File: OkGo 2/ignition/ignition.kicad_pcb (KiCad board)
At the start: 2 copper layers, 167.9 x 105.9 mm, 112 parts, among them K201 16A SPST, K202 16A SPST, K203 16A SPST, K204 16A SPST, K205 16A SPST, M3_MOUNT VAL**, P105 BATT, P107 ARM_LED, P109 BUZZ, P111 SMA, P201 CH3_LED, P203 CH3, P204 CH1_LED, P206 CH1, P207 CH4_LED, P209 CH4, P210 CH2_LED, P212 CH2, Q101 BSS138BK, Q201 BSS138BK, Q202 BSS138BK, Q203 BSS138BK, Q204 BSS138BK, Q205 BSS138BK, U103 SWD, U105 RFM95W, U106 STM32F071CBT6, U107 TSR 0.5-2433, Y101 8MHz

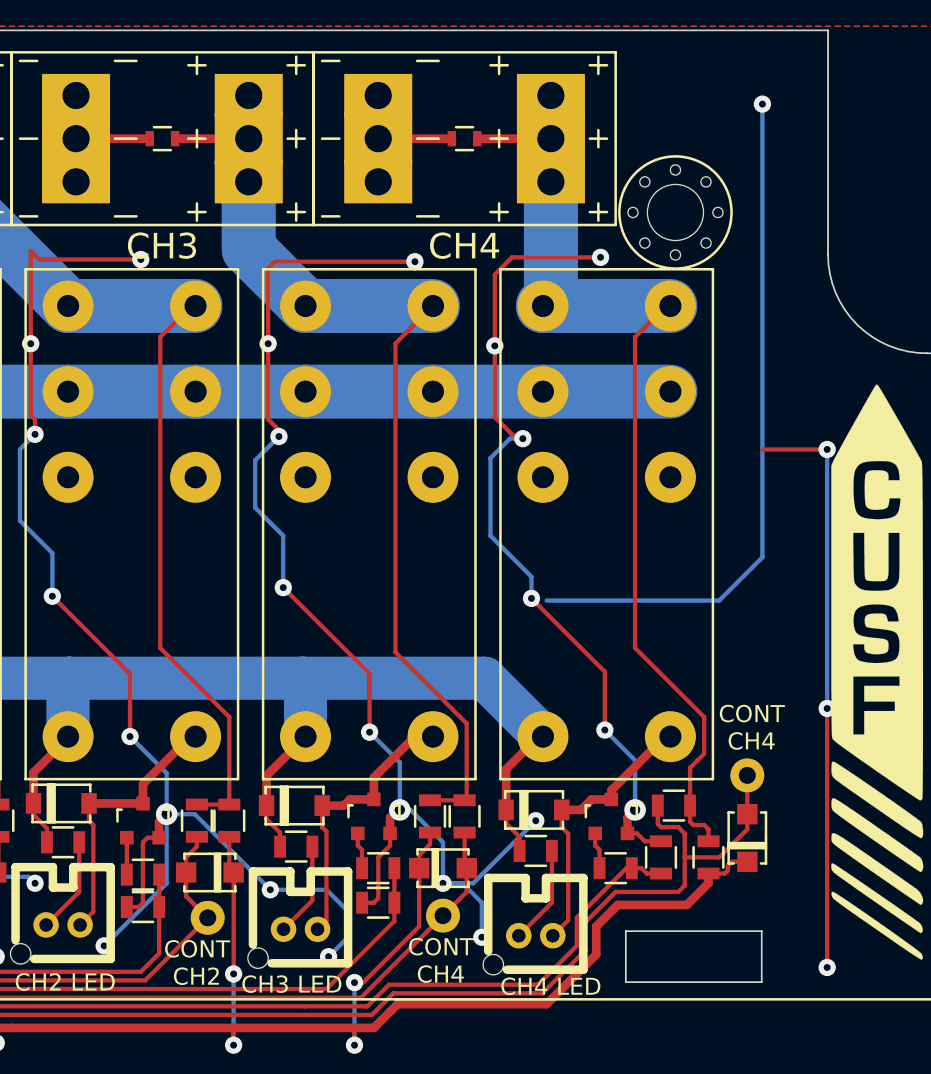
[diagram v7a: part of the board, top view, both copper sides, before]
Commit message: Fixed stitching derp. resolves #31
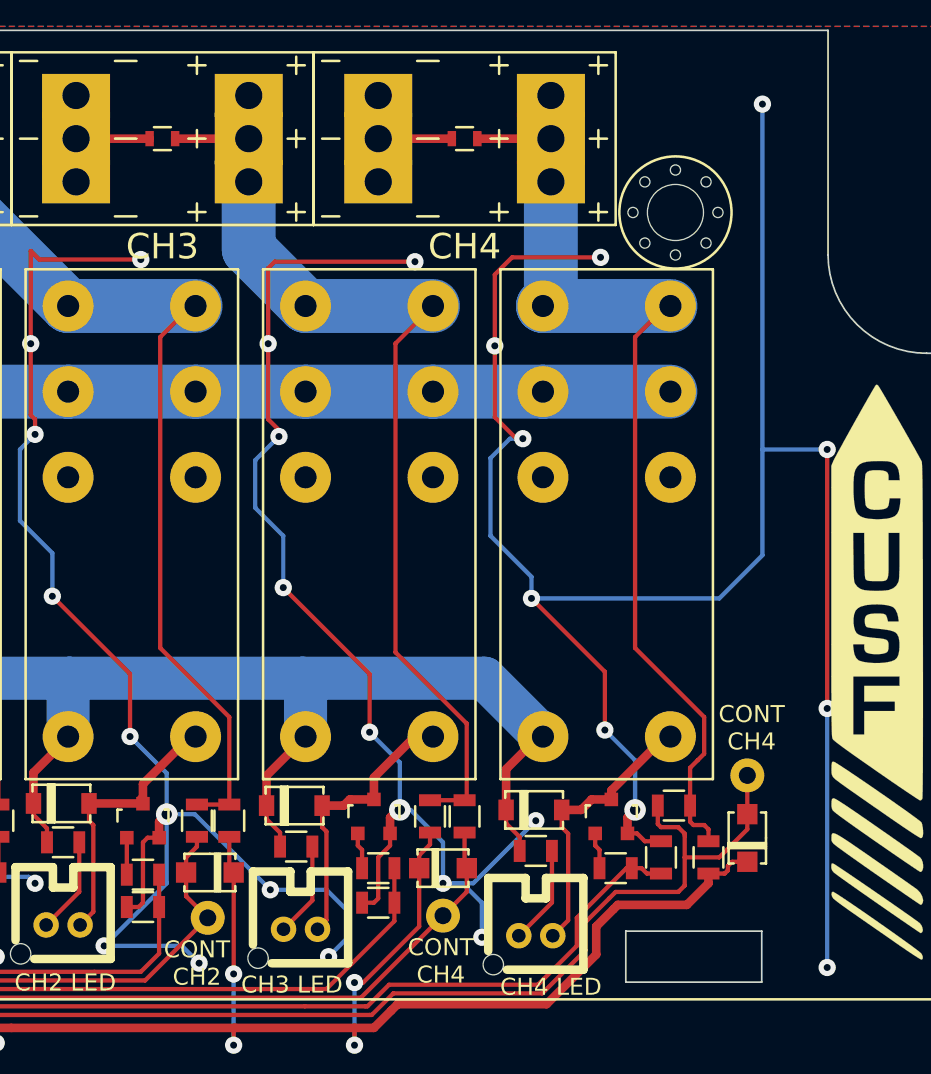
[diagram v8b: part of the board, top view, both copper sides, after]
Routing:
- net GND: track 1436.7 -> 1518.1 mm, vias 150 -> 155
- net (no net): track 74.7 -> 0.00 mm, vias 4 -> 0
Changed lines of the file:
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@@
     (thickness 1.6)
     (drawings 67)
-    (tracks 1581)
+    (tracks 1585)
     (zones 0)
     (modules 112)
@@
   (gr_arc (start 41.2 141.7) (end 41.2 135.9) (angle 90) (layer Edge.Cuts) (width 0.1))
   (gr_line (start 38 68) (end 38 135.9) (angle 90) (layer Edge.Cuts) (width 0.1))
-  (via (at 196.85 88.9) (size 1.016) (drill 0.4064) (layers F.Cu B.Cu) (net 0))
-  (via (at 196.85 73.66) (size 1.016) (drill 0.4064) (layers F.Cu B.Cu) (net 0))
-  (segment (start 193.04 73.66) (end 196.85 73.66) (width 0.254) (layer F.Cu) (net 0))
-  (segment (start 196.85 88.9) (end 196.85 73.66) (width 0.254) (layer B.Cu) (net 0))
-  (via (at 196.85 104.14) (size 1.016) (drill 0.4064) (layers F.Cu B.Cu) (net 0))
-  (segment (start 196.85 88.9) (end 196.85 104.14) (width 0.254) (layer F.Cu) (net 0))
-  (segment (start 180.34 82.55) (end 190.5 82.55) (width 0.254) (layer B.Cu) (net 0))
-  (via (at 193.04 53.34) (size 1.016) (drill 0.4064) (layers F.Cu B.Cu) (net 0))
-  (segment (start 193.04 80.01) (end 193.04 53.34) (width 0.254) (layer B.Cu) (net 0))
-  (segment (start 190.5 82.55) (end 193.04 80.01) (width 0.254) (layer B.Cu) (net 0))
   (segment (start 71.442 81.07) (end 72.434 81.07) (width 0.254) (layer F.Cu) (net 1))
   (segment (start 78.486 81.153) (end 78.486 81.083002) (width 0.254) (layer F.Cu) (net 1))
@@
   (segment (start 51.689 77.724) (end 52.451 78.486) (width 1.016) (layer F.Cu) (net 1))
   (segment (start 43.688 77.724) (end 43.688 77.851) (width 1.524) (layer F.Cu) (net 1))
+  (segment (start 154.305 102.87) (end 158.877 102.87) (width 0.254) (layer B.Cu) (net 2))
+  (segment (start 157.988 99.187) (end 154.305 102.87) (width 0.254) (layer B.Cu) (net 2))
+  (via (at 154.305 102.87) (size 1.016) (drill 0.4064) (layers F.Cu B.Cu) (net 2))
+  (segment (start 157.988 95.123) (end 157.988 99.187) (width 0.254) (layer B.Cu) (net 2))
+  (via (at 159.893 103.886) (size 1.016) (drill 0.4064) (layers F.Cu B.Cu) (net 2))
+  (segment (start 158.877 102.87) (end 159.893 103.886) (width 0.254) (layer B.Cu) (net 2))
+  (segment (start 193.04 73.66) (end 196.85 73.66) (width 0.254) (layer B.Cu) (net 2))
+  (via (at 196.85 104.14) (size 1.016) (drill 0.4064) (layers F.Cu B.Cu) (net 2))
+  (segment (start 196.85 88.9) (end 196.85 104.14) (width 0.254) (layer B.Cu) (net 2))
+  (via (at 196.85 88.9) (size 1.016) (drill 0.4064) (layers F.Cu B.Cu) (net 2))
+  (segment (start 196.85 73.66) (end 196.85 88.9) (width 0.254) (layer F.Cu) (net 2))
+  (via (at 196.85 73.66) (size 1.016) (drill 0.4064) (layers F.Cu B.Cu) (net 2))
+  (segment (start 179.451 82.423) (end 190.5 82.423) (width 0.254) (layer B.Cu) (net 2))
+  (via (at 193.04 53.34) (size 1.016) (drill 0.4064) (layers F.Cu B.Cu) (net 2))
+  (segment (start 193.04 79.883) (end 193.04 73.66) (width 0.254) (layer B.Cu) (net 2))
+  (segment (start 193.04 73.66) (end 193.04 53.34) (width 0.254) (layer B.Cu) (net 2))
+  (segment (start 190.5 82.423) (end 193.04 79.883) (width 0.254) (layer B.Cu) (net 2))
   (segment (start 146.558 98.806) (end 149.86 98.806) (width 0.254) (layer B.Cu) (net 2))
   (segment (start 146.177 99.187) (end 146.558 98.806) (width 0.254) (layer B.Cu) (net 2))
@@
   (segment (start 150.495 62.484) (end 156.464 62.484) (width 0.254) (layer F.Cu) (net 2))
   (segment (start 149.987 61.976) (end 150.495 62.484) (width 0.254) (layer F.Cu) (net 2))
-  (segment (start 157.988 95.123) (end 157.988 99.187) (width 0.254) (layer B.Cu) (net 2))
   (via (at 157.988 95.123) (size 1.27) (drill 0.6096) (layers F.Cu B.Cu) (net 2))
   (segment (start 157.541 95.57) (end 157.988 95.123) (width 0.508) (layer F.Cu) (net 2))
   (segment (start 157.541 96.50476) (end 157.541 95.57) (width 0.508) (layer F.Cu) (net 2))
-  (via (at 154.305 102.87) (size 1.016) (drill 0.4064) (layers F.Cu B.Cu) (net 2))
-  (segment (start 157.988 99.187) (end 154.305 102.87) (width 0.254) (layer B.Cu) (net 2))
   (segment (start 139.573 102.108) (end 144.907 102.108) (width 0.254) (layer B.Cu) (net 2))
   (segment (start 140.081 97.663) (end 141.097 98.679) (width 0.254) (layer B.Cu) (net 2))
